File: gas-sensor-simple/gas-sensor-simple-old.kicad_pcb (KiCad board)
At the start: 2 copper layers, 97.8 x 99.1 mm, 47 parts, among them J1 RPi, J2 digital header, J3 digital header, J4 1x2, J5 1x2, J6 1x2, J7 1x2, U1 MQ-8, U10 RG LED, U12 LM393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

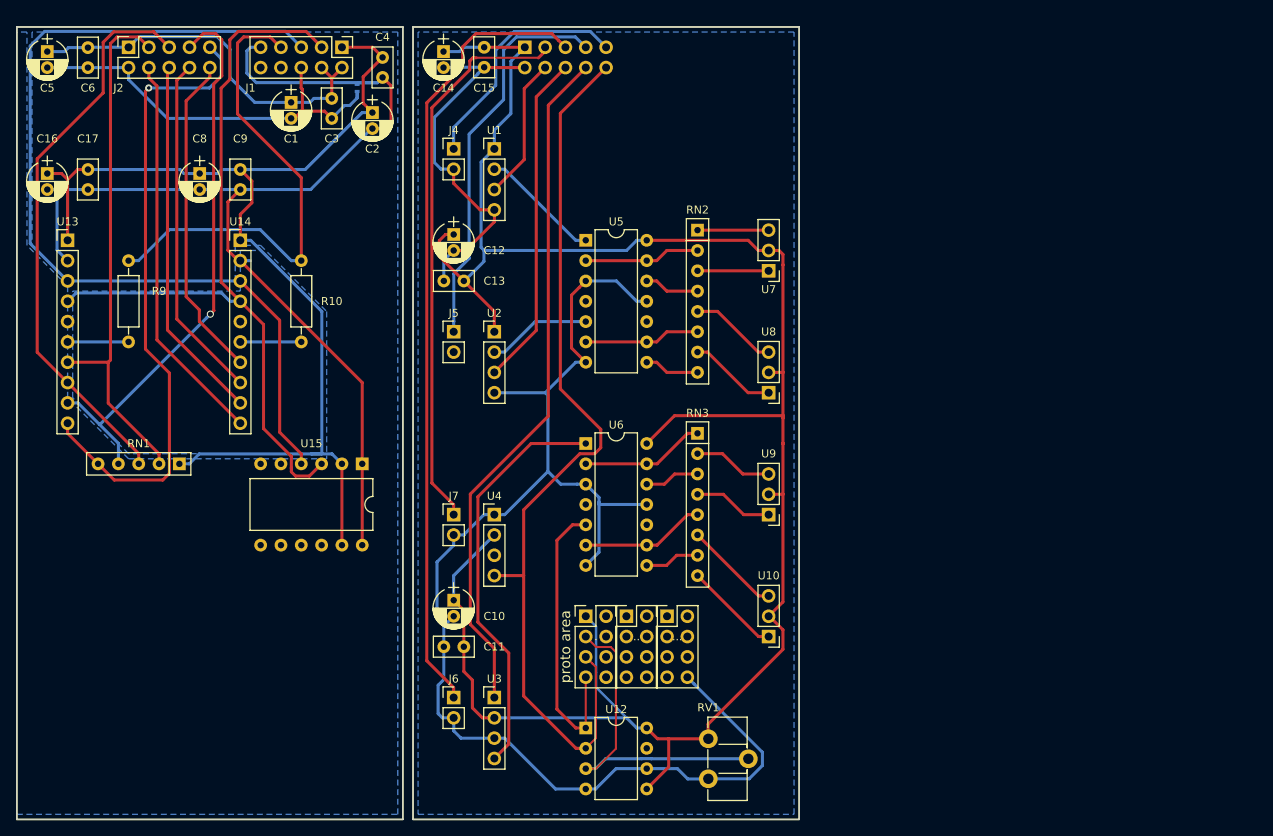
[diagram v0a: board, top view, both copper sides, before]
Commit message: Add ground planes. Create new gerbers in layout2.gerbers.
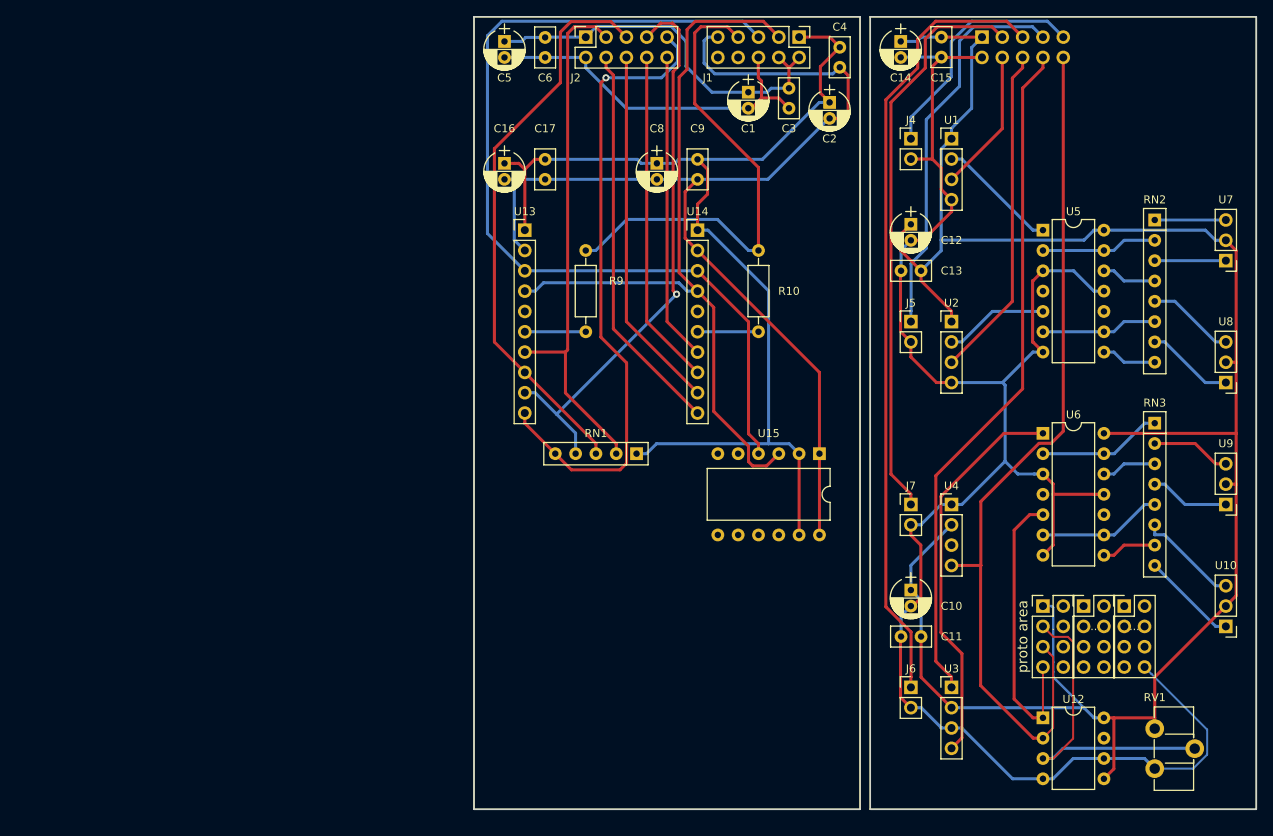
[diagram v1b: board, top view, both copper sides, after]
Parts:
- removed JP1: ., Resistors_SMD:R_0402_NoSilk
- moved . 57.2 mm to (227.3, 124.5)
- moved .. 57.2 mm to (232.4, 124.5)
- moved ... 57.2 mm to (237.5, 124.5)
- moved C1 57.2 mm to (190.5, 60.2)
- moved C10 57.2 mm to (210.8, 122.5)
- moved C11 57.2 mm to (209.6, 128.3)
- moved C12 57.2 mm to (210.8, 76.7)
- moved C13 57.2 mm to (209.6, 82.5)
- moved C14 57.2 mm to (209.6, 53.9)
- moved C15 57.2 mm to (214.6, 55.8)
- moved C16 57.2 mm to (160.0, 69.1)
- moved C2 57.2 mm to (200.7, 61.5)
- moved C3 57.2 mm to (195.6, 62.2)
- moved C4 57.2 mm to (201.9, 57.1)
- moved C5 57.2 mm to (160.0, 53.9)
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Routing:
- net VCC: track 312.7 -> 304.2 mm
- net GNDD: track 141.3 -> 136.5 mm
- net Net-(J3-Pad10): track 114.7 -> 110.3 mm
- net GND: track 269.4 -> 272.0 mm
- net Net-(J2-Pad10): track 40.9 -> 38.4 mm
- net Net-(U3-Pad4): track 51.3 -> 49.1 mm
- net +3V3: track 140.9 -> 138.9 mm
- net Net-(J3-Pad3): track 70.2 -> 71.8 mm
- net Net-(J2-Pad8): track 43.3 -> 42.0 mm
- net Net-(RV1-Pad2): track 42.3 -> 41.0 mm
- net Net-(J3-Pad8): track 86.0 -> 85.1 mm
- net Net-(RN3-Pad6): track 12.0 -> 12.8 mm
- removed copper zone on B.Cu, net GND
- removed copper zone on B.Cu, net GNDD
